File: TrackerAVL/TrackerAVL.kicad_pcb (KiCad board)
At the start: 2 copper layers, 120 x 80 mm, 173 parts, among them J801 Conn_02x07_Odd_Even, J802 Conn_01x15, J803 Conn_01x04, P201 uC_debug, Q201 DTC043ZEBTL, Q202 DTC043ZEBTL, Q203 DTC043ZEBTL, Q701 2N7002P, Q702 2N7002P, Q703 2N7002P, Q704 DTC043ZEBTL, U201 MAX3221, U202 LPC4337JBD144, U203 STS8C5H30L, U301 MPU-6050, U401 NAU8814, U501 STS8C5H30L, U502 LD1085D2T33R, U503 NCP114ASN180T1G, U601 MPCIE-Socket, U701 74LVC244APW, U801 74HC4053, X201 12MHz, X202 32.768K

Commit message: PCB terminado, para su revisión final
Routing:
- net +3V3: track 639.7 -> 637.7 mm
- net GND: track 507.3 -> 508.2 mm, vias 59 -> 60
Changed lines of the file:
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@@
-(kicad_pcb (version 20171130) (host pcbnew "(5.0.0)")
+(kicad_pcb (version 20171130) (host pcbnew 5.0.1-33cea8e~68~ubuntu16.04.1)
   (general
     (thickness 1.6)
     (drawings 31)
-    (tracks 2799)
+    (tracks 2800)
     (zones 0)
     (modules 173)
@@
   )
   (setup
-    (last_trace_width 0.25)
+    (last_trace_width 0.2)
     (user_trace_width 0.2)
     (user_trace_width 0.24)
@@
   (via (at 81.925 35.275) (size 0.8) (drill 0.4) (layers F.Cu B.Cu) (net 1))
   (segment (start 84.923794 34.58514) (end 82.61486 34.58514) (width 0.25) (layer F.Cu) (net 1))
-  (segment (start 85.419496 34.58514) (end 84.923794 34.58514) (width 0.25) (layer F.Cu) (net 1))
-  (segment (start 85.678804 34.325832) (end 85.419496 34.58514) (width 0.25) (layer F.Cu) (net 1))
-  (segment (start 85.678804 33.844448) (end 85.678804 34.325832) (width 0.25) (layer F.Cu) (net 1))
-  (segment (start 85.419496 33.58514) (end 85.678804 33.844448) (width 0.25) (layer F.Cu) (net 1))
-  (segment (start 84.923794 33.58514) (end 85.419496 33.58514) (width 0.25) (layer F.Cu) (net 1))
   (segment (start 78.55 36.5) (end 78.55 34.475) (width 0.25) (layer F.Cu) (net 1))
   (via (at 80.423794 31.83514) (size 0.8) (drill 0.4) (layers F.Cu B.Cu) (net 1))
@@
   (segment (start 99.75 35.575) (end 99.75 35.05) (width 0.25) (layer F.Cu) (net 1))
   (segment (start 99.75 35.05) (end 100.27501 34.52499) (width 0.25) (layer F.Cu) (net 1))
+  (via (at 81.925 33.425) (size 0.8) (drill 0.4) (layers F.Cu B.Cu) (net 1))
+  (segment (start 84.923794 33.58514) (end 82.08514 33.58514) (width 0.2) (layer F.Cu) (net 1))
+  (segment (start 82.08514 33.58514) (end 81.925 33.425) (width 0.2) (layer F.Cu) (net 1))
   (via (at 73 82) (size 0.8) (drill 0.4) (layers F.Cu B.Cu) (net 2))
   (via (at 71 82) (size 0.8) (drill 0.4) (layers F.Cu B.Cu) (net 2))
@@
   (segment (start 79.875 36.5) (end 80.6 36.5) (width 0.25) (layer F.Cu) (net 2))
   (segment (start 79.55 36.175) (end 79.875 36.5) (width 0.25) (layer F.Cu) (net 2))
-  (segment (start 84.923794 33.08514) (end 80.137862 33.08514) (width 0.25) (layer F.Cu) (net 2))
   (segment (start 79.55 33.673002) (end 79.55 36.175) (width 0.25) (layer F.Cu) (net 2))
   (segment (start 80.137862 33.08514) (end 79.55 33.673002) (width 0.25) (layer F.Cu) (net 2))
@@
   (segment (start 80.701206 38.048794) (end 85.623794 38.048794) (width 0.25) (layer F.Cu) (net 2))
   (segment (start 80.6 38.15) (end 80.701206 38.048794) (width 0.25) (layer F.Cu) (net 2))
-  (segment (start 82.473794 30.65) (end 82.473794 33.058934) (width 0.25) (layer F.Cu) (net 2))
-  (segment (start 82.5 33.08514) (end 84.923794 33.08514) (width 0.25) (layer F.Cu) (net 2))
-  (segment (start 82.473794 33.058934) (end 82.5 33.08514) (width 0.25) (layer F.Cu) (net 2))
   (segment (start 135.700319 52.7) (end 129.25 52.7) (width 0.25) (layer B.Cu) (net 2))
   (segment (start 137.376545 54.3) (end 137.300319 54.3) (width 0.25) (layer B.Cu) (net 2))
@@
   (segment (start 90 39.7) (end 89.225 39.7) (width 0.25) (layer F.Cu) (net 2))
   (segment (start 89.225 39.7) (end 89 39.475) (width 0.25) (layer F.Cu) (net 2))
+  (segment (start 80.548003 32.674999) (end 80.137862 33.08514) (width 0.2) (layer F.Cu) (net 2))
+  (segment (start 82.399999 32.674999) (end 80.548003 32.674999) (width 0.2) (layer F.Cu) (net 2))
+  (segment (start 82.473794 32.601204) (end 82.399999 32.674999) (width 0.2) (layer F.Cu) (net 2))
+  (segment (start 82.473794 30.2) (end 82.473794 32.601204) (width 0.2) (layer F.Cu) (net 2))
+  (segment (start 82.599999 32.674999) (end 82.399999 32.674999) (width 0.2) (layer F.Cu) (net 2))
+  (segment (start 84.923794 33.08514) (end 83.01014 33.08514) (width 0.2) (layer F.Cu) (net 2))
+  (segment (start 83.01014 33.08514) (end 82.599999 32.674999) (width 0.2) (layer F.Cu) (net 2))
   (segment (start 101.60426 63.62074) (end 101.525 63.7) (width 0.24) (layer F.Cu) (net 3))
   (segment (start 101.60426 60.25182) (end 101.60426 63.62074) (width 0.24) (layer F.Cu) (net 3))
@@
   (segment (start 120.5 52.755) (end 119.78 52.755) (width 0.25) (layer F.Cu) (net 19))
   (segment (start 119.78 52.755) (end 119.5 52.475) (width 0.25) (layer F.Cu) (net 19))
-  (segment (start 81.96486 34.08514) (end 84.923794 34.08514) (width 0.25) (layer F.Cu) (net 20))
-  (segment (start 80.6 34.475) (end 81.575 34.475) (width 0.25) (layer F.Cu) (net 20))
-  (segment (start 81.575 34.475) (end 81.96486 34.08514) (width 0.25) (layer F.Cu) (net 20))
+  (segment (start 82.33986 34.08514) (end 84.923794 34.08514) (width 0.25) (layer F.Cu) (net 20))
+  (segment (start 80.6 34.475) (end 81.95 34.475) (width 0.25) (layer F.Cu) (net 20))
+  (segment (start 81.95 34.475) (end 82.33986 34.08514) (width 0.25) (layer F.Cu) (net 20))
   (segment (start 90.9 34.775) (end 90.71014 34.58514) (width 0.25) (layer F.Cu) (net 21))
   (segment (start 90.9 35.25) (end 90.9 34.775) (width 0.25) (layer F.Cu) (net 21))

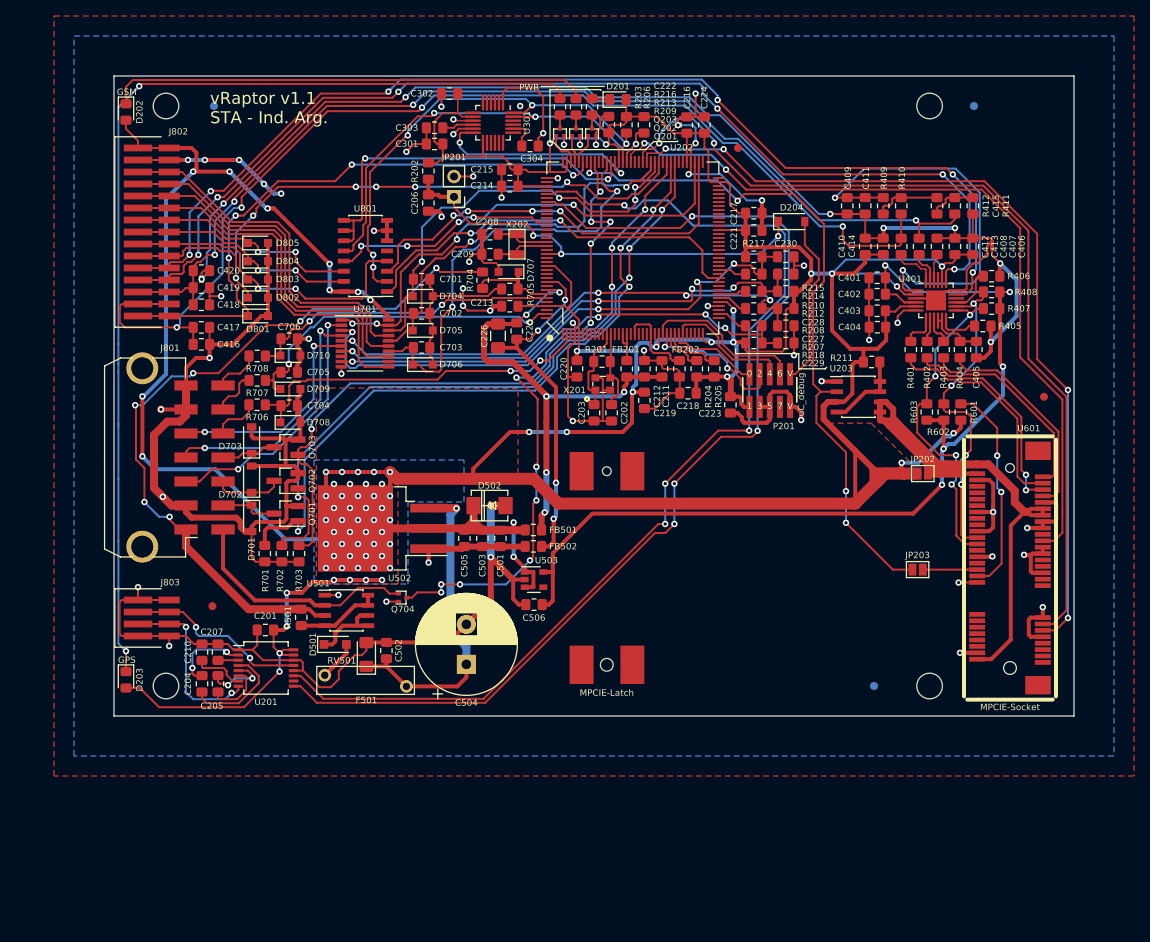
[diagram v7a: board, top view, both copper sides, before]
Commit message: Cambios en README, ahora incluye información de versiones
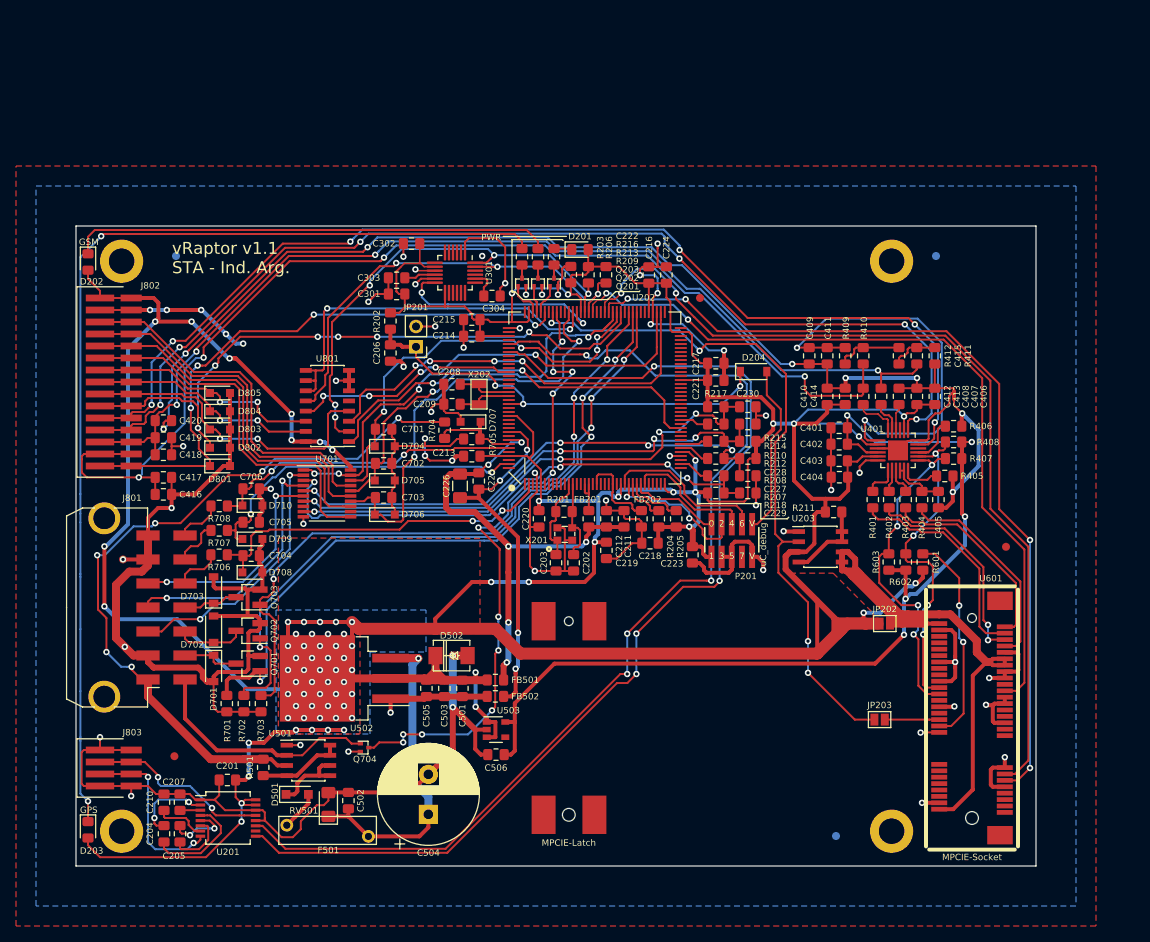
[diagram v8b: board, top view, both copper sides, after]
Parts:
- H101, H102, H103, H104: footprint MountingHole:MountingHole_3.2mm_M3 -> MountingHole:MountingHole_3.2mm_M3_Pad_Thin
- moved H104 20.2 mm to (40.5, 51.1)
- moved H102 20.0 mm to (136.7, 51.1)
- moved C208 19.3 mm to (81.8, 66.5)
- moved C209 19.3 mm to (81.8, 69.0)
- moved C213 19.3 mm to (84.2, 75.5)
- moved C402 19.3 mm to (130.2, 74.0)
- moved C404 19.3 mm to (130.2, 78.2)
- moved C419 19.3 mm to (45.7, 73.2)
- moved C701 19.3 mm to (73.2, 72.2)
- moved D705 19.3 mm to (73.3, 78.6)
- moved JP401 19.3 mm to (144.5, 67.9)
- moved R406 19.3 mm to (144.4, 71.8)
- moved R704 19.3 mm to (80.8, 72.3)
- moved X202 19.3 mm to (85.1, 66.5)
- moved C302 19.3 mm to (76.7, 49.0)
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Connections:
- P201 pad 7: (no net) -> Net-(P201-Pad7)
- U201 pad 10: (no net) -> Net-(U201-Pad10)
- U202 pad 1: (no net) -> Net-(U202-Pad1)
- U202 pad 10: (no net) -> Net-(U202-Pad10)
- U202 pad 102: (no net) -> Net-(U202-Pad102)
- U202 pad 108: (no net) -> Net-(U202-Pad108)
- U202 pad 11: (no net) -> Net-(U202-Pad11)
- U202 pad 110: (no net) -> Net-(U202-Pad110)
- U202 pad 112: (no net) -> Net-(U202-Pad112)
- U202 pad 114: (no net) -> Net-(U202-Pad114)
- U202 pad 116: (no net) -> Net-(U202-Pad116)
- U202 pad 117: (no net) -> Net-(U202-Pad117)
- U202 pad 118: (no net) -> Net-(U202-Pad118)
- U202 pad 119: (no net) -> Net-(U202-Pad119)
- U202 pad 121: (no net) -> Net-(U202-Pad121)
- U202 pad 122: (no net) -> Net-(U202-Pad122)
- U202 pad 123: (no net) -> Net-(U202-Pad123)
- U202 pad 124: (no net) -> Net-(U202-Pad124)
- U202 pad 127: (no net) -> Net-(U202-Pad127)
- U202 pad 129: (no net) -> Net-(U202-Pad129)
- U202 pad 130: (no net) -> Net-(U202-Pad130)
- U202 pad 132: (no net) -> Net-(U202-Pad132)
- U202 pad 133: (no net) -> Net-(U202-Pad133)
- U202 pad 134: (no net) -> Net-(U202-Pad134)
- U202 pad 136: (no net) -> Net-(U202-Pad136)
- U202 pad 14: (no net) -> Net-(U202-Pad14)
- U202 pad 140: (no net) -> Net-(U202-Pad140)
- U202 pad 142: (no net) -> Net-(U202-Pad142)
- U202 pad 144: (no net) -> Net-(U202-Pad144)
- U202 pad 15: (no net) -> Net-(U202-Pad15)
- U202 pad 18: (no net) -> Net-(U202-Pad18)
- U202 pad 20: (no net) -> Net-(U202-Pad20)
- U202 pad 21: (no net) -> Net-(U202-Pad21)
- U202 pad 22: (no net) -> Net-(U202-Pad22)
- U202 pad 24: (no net) -> Net-(U202-Pad24)
- U202 pad 3: (no net) -> Net-(U202-Pad3)
- U202 pad 32: (no net) -> Net-(U202-Pad32)
- U202 pad 33: (no net) -> Net-(U202-Pad33)
- U202 pad 34: (no net) -> Net-(U202-Pad34)
- U202 pad 35: (no net) -> Net-(U202-Pad35)
- U202 pad 37: (no net) -> Net-(U202-Pad37)
- U202 pad 39: (no net) -> Net-(U202-Pad39)
- U202 pad 44: (no net) -> Net-(U202-Pad44)
- U202 pad 45: (no net) -> Net-(U202-Pad45)
- U202 pad 46: (no net) -> Net-(U202-Pad46)
- U202 pad 48: (no net) -> Net-(U202-Pad48)
- U202 pad 50: (no net) -> Net-(U202-Pad50)
- U202 pad 51: (no net) -> Net-(U202-Pad51)
- U202 pad 52: (no net) -> Net-(U202-Pad52)
- U202 pad 53: (no net) -> Net-(U202-Pad53)
- U202 pad 54: (no net) -> Net-(U202-Pad54)
- U202 pad 55: (no net) -> Net-(U202-Pad55)
- U202 pad 56: (no net) -> Net-(U202-Pad56)
- U202 pad 57: (no net) -> Net-(U202-Pad57)
- U202 pad 58: (no net) -> Net-(U202-Pad58)
- U202 pad 6: (no net) -> Net-(U202-Pad6)
- U202 pad 60: (no net) -> Net-(U202-Pad60)
- U202 pad 61: (no net) -> Net-(U202-Pad61)
- U202 pad 62: (no net) -> Net-(U202-Pad62)
- U202 pad 63: (no net) -> Net-(U202-Pad63)
- U202 pad 64: (no net) -> Net-(U202-Pad64)
- U202 pad 65: (no net) -> Net-(U202-Pad65)
- U202 pad 66: (no net) -> Net-(U202-Pad66)
- U202 pad 67: (no net) -> Net-(U202-Pad67)
- U202 pad 68: (no net) -> Net-(U202-Pad68)
- U202 pad 69: (no net) -> Net-(U202-Pad69)
- U202 pad 7: (no net) -> Net-(U202-Pad7)
- U202 pad 70: (no net) -> Net-(U202-Pad70)
- U202 pad 72: (no net) -> Net-(U202-Pad72)
- U202 pad 73: (no net) -> Net-(U202-Pad73)
- U202 pad 78: (no net) -> Net-(U202-Pad78)
- U202 pad 79: (no net) -> Net-(U202-Pad79)
- U202 pad 8: (no net) -> Net-(U202-Pad8)
- U202 pad 83: (no net) -> Net-(U202-Pad83)
- U202 pad 89: (no net) -> Net-(U202-Pad89)
- U202 pad 9: (no net) -> Net-(U202-Pad9)
- U202 pad 90: (no net) -> Net-(U202-Pad90)
- U202 pad 98: (no net) -> Net-(U202-Pad98)
- U202 pad 99: (no net) -> Net-(U202-Pad99)
- U301 pad 6: (no net) -> Net-(U301-Pad6)
- U301 pad 7: (no net) -> Net-(U301-Pad7)
- U401 pad 16: (no net) -> Net-(U401-Pad16)
- U401 pad 21: (no net) -> Net-(U401-Pad21)
- U601 pad 1: (no net) -> Net-(U601-Pad1)
- U601 pad 10: (no net) -> Net-(U601-Pad10)
- U601 pad 12: (no net) -> Net-(U601-Pad12)
- U601 pad 14: (no net) -> Net-(U601-Pad14)
- U601 pad 16: (no net) -> Net-(U601-Pad16)
- U601 pad 17: (no net) -> Net-(U601-Pad17)
- U601 pad 19: (no net) -> Net-(U601-Pad19)
- U601 pad 23: (no net) -> Net-(U601-Pad23)
- U601 pad 24: (no net) -> Net-(U601-Pad24)
- U601 pad 25: (no net) -> Net-(U601-Pad25)
- U601 pad 28: (no net) -> Net-(U601-Pad28)
- U601 pad 3: (no net) -> Net-(U601-Pad3)
- U601 pad 33: (no net) -> Net-(U601-Pad33)
- U601 pad 36: (no net) -> Net-(U601-Pad36)
- U601 pad 38: (no net) -> Net-(U601-Pad38)
- U601 pad 42: (no net) -> Net-(U601-Pad42)
- U601 pad 44: (no net) -> Net-(U601-Pad44)
- U601 pad 46: (no net) -> Net-(U601-Pad46)
- U601 pad 48: (no net) -> Net-(U601-Pad48)
- U601 pad 5: (no net) -> Net-(U601-Pad5)
- U601 pad 6: (no net) -> Net-(U601-Pad6)
- U601 pad 7: (no net) -> Net-(U601-Pad7)
- U601 pad 8: (no net) -> Net-(U601-Pad8)
- U701 pad 12: (no net) -> Net-(U701-Pad12)
- U701 pad 8: (no net) -> Net-(U701-Pad8)
- U801 pad 5: (no net) -> Net-(U801-Pad5)
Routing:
- net +3V3: track 637.7 -> 638.2 mm
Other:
- board text removed: "A modificar en v1.1: > Pistas que acceden a pads, que sea a 90°, y lo más estranguladas posibles (grosor pista << grosor pad). > Pistas que entren/salen de un mismo componente, que sean homogeneas (mismo ancho). > Pads QFN alargarlos, para facilitar el soldado. El ta- maño del pad aprox. 1.5mm (ese es el ancho de la superficie del pad que la punta del soldador debe hacer contacto -punta 900m-t-2c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"
- board text removed: "A modificar en v1.2: > Modificar huellas para que posean el área que las delimita, así se valida el ERC en forma integral (con todos los checks activados). > Ver otros errores del ERC integral. > Ver posibilidad de que existan componentes en ambas capas. > Verificar diseño de v1.1 y corregir errores en caso de que existan."
